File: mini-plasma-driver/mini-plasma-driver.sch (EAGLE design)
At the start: 92 parts, among them IC1 IR21844D, IC2 74LS19N, IC3 NE555N, IC5 IR21844D, J1 12v IN, Q1 STH60N10W, Q3 2N2369, Q4 2N2369, Q7 STH60N10W, Q8 STH60N10W, Q9 STH60N10W

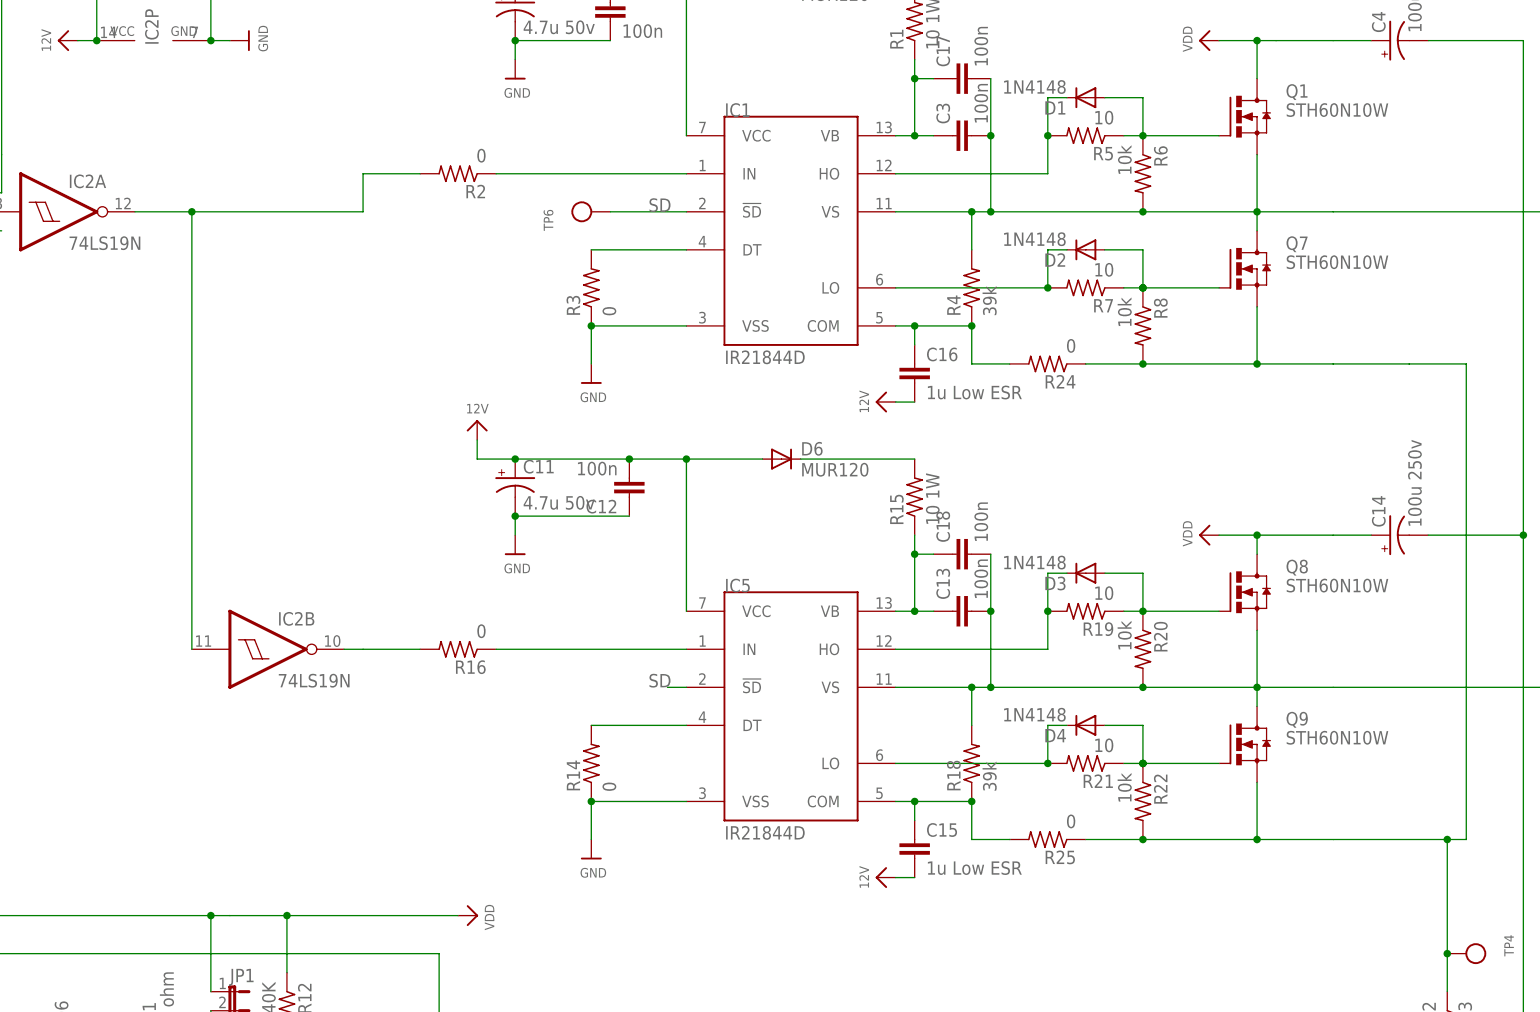
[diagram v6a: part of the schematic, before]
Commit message: Rotated driver chips and compleeted routing; Still have air wires remaining. Unclear what else need to be done.
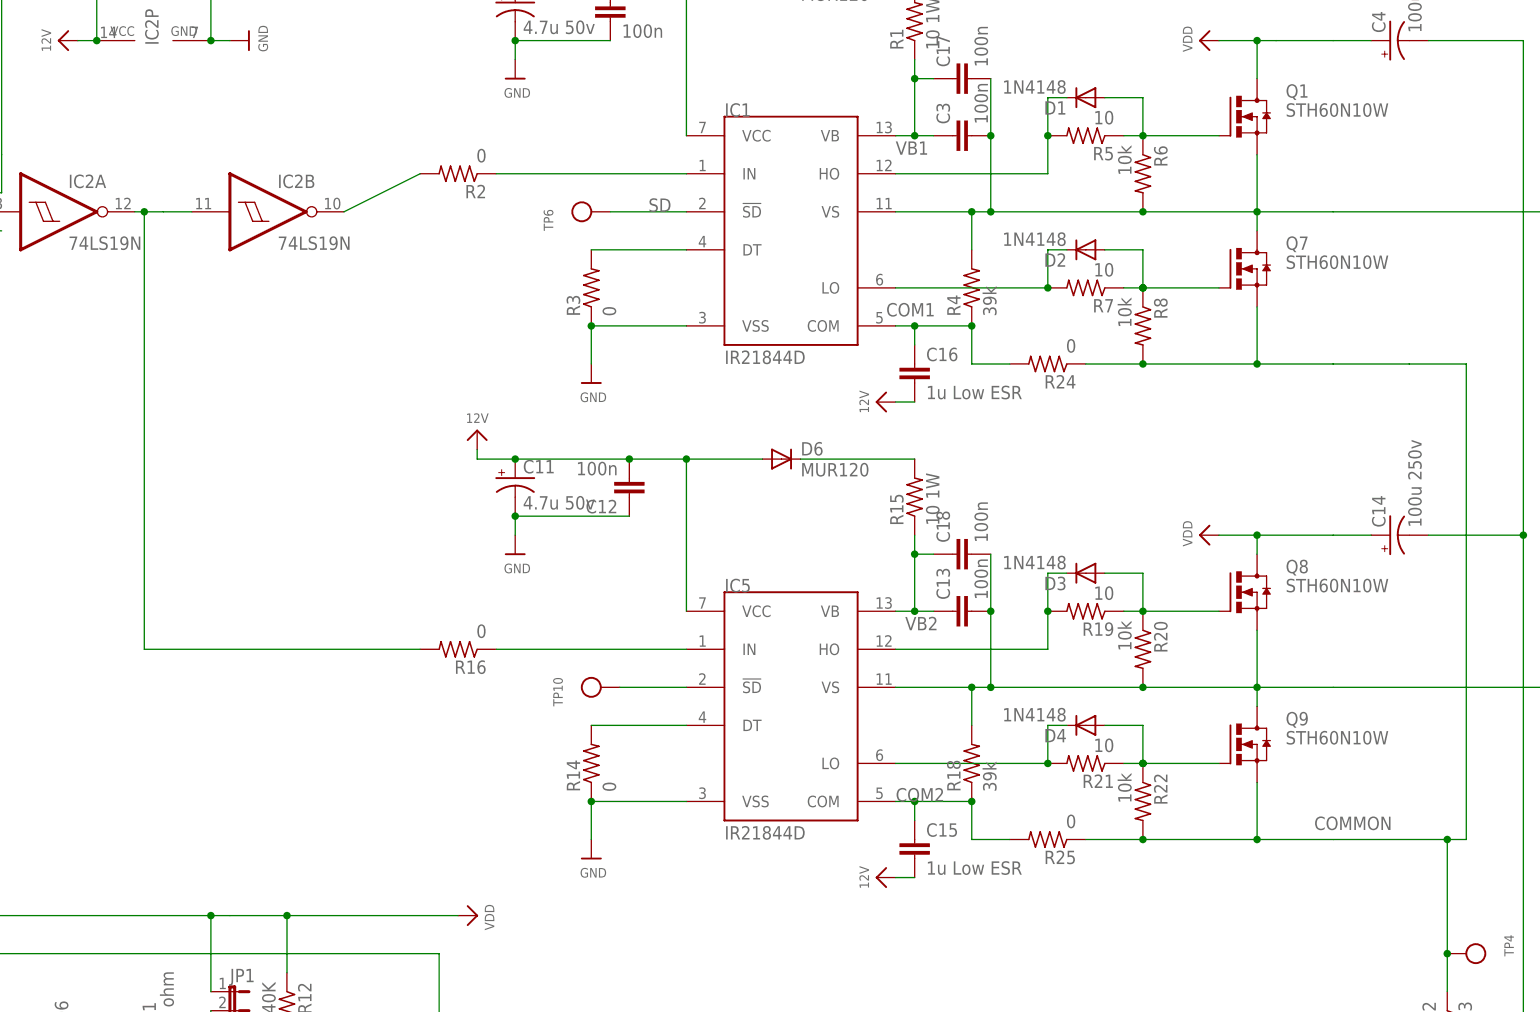
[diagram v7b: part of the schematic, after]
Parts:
- added TP10: (no value), microbuilder:TESTPOINT0.1"
- C15, C16: device rcl:C-EU050-035X075 -> rcl:C-EU025-025X050
- C2: device rcl:C-EU025-030X050 -> rcl:C-EU025-025X050
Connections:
- net N$35 renamed COMMON
- net VDD renamed VDD+
- removed net COM: C15.1, C16.1, IC1.COM, IC5.COM, R18.1, R24.2, R25.2, R4.1
- removed net N$24: IC2B.O, R16.2
- removed net VB: C13.1, C17.1, C18.1, C3.1, IC1.VB, IC5.VB, R1.1, R15.1
- new net COM1: C16.1, IC1.COM, R24.2, R4.1
- new net COM2: C15.1, IC5.COM, R18.1, R25.2
- new net N$33: IC5.!SD, TP10.P$1
- new net N$36: IC2A.O, IC2B.I, R16.2
- new net VB1: C17.1, C3.1, IC1.VB, R1.1
- new net VB2: C13.1, C18.1, IC5.VB, R15.1
- net N$4: now also IC2B.O; no longer IC2A.O, IC2B.I
- net SD: no longer IC5.!SD
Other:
- moved on the sheet: IC2B

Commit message: update TP11 to through hole, fix airwires
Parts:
- TP11: device microbuilder:TESTPOINTROUND2MM -> microbuilder:TESTPOINT0.1"
